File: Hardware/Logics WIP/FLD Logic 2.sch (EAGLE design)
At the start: 82 parts

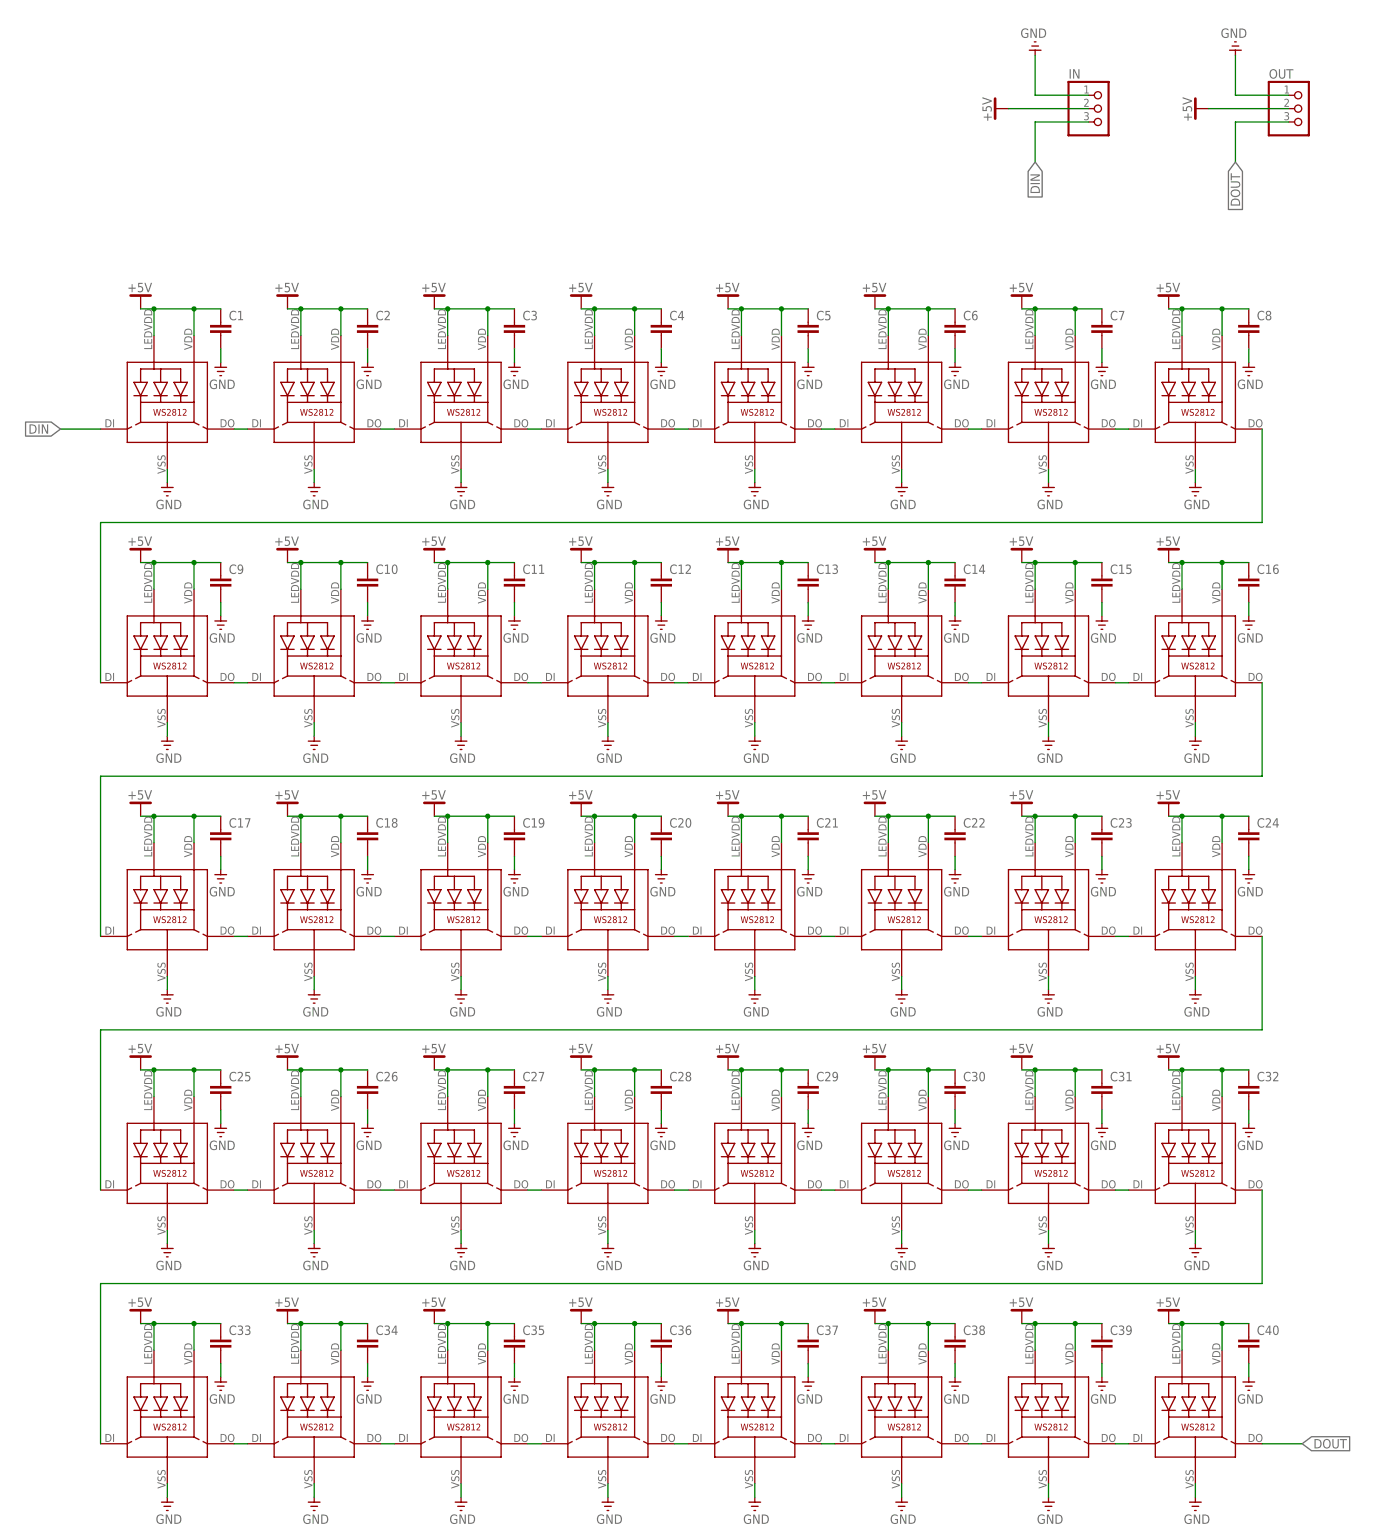
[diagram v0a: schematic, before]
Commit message: 
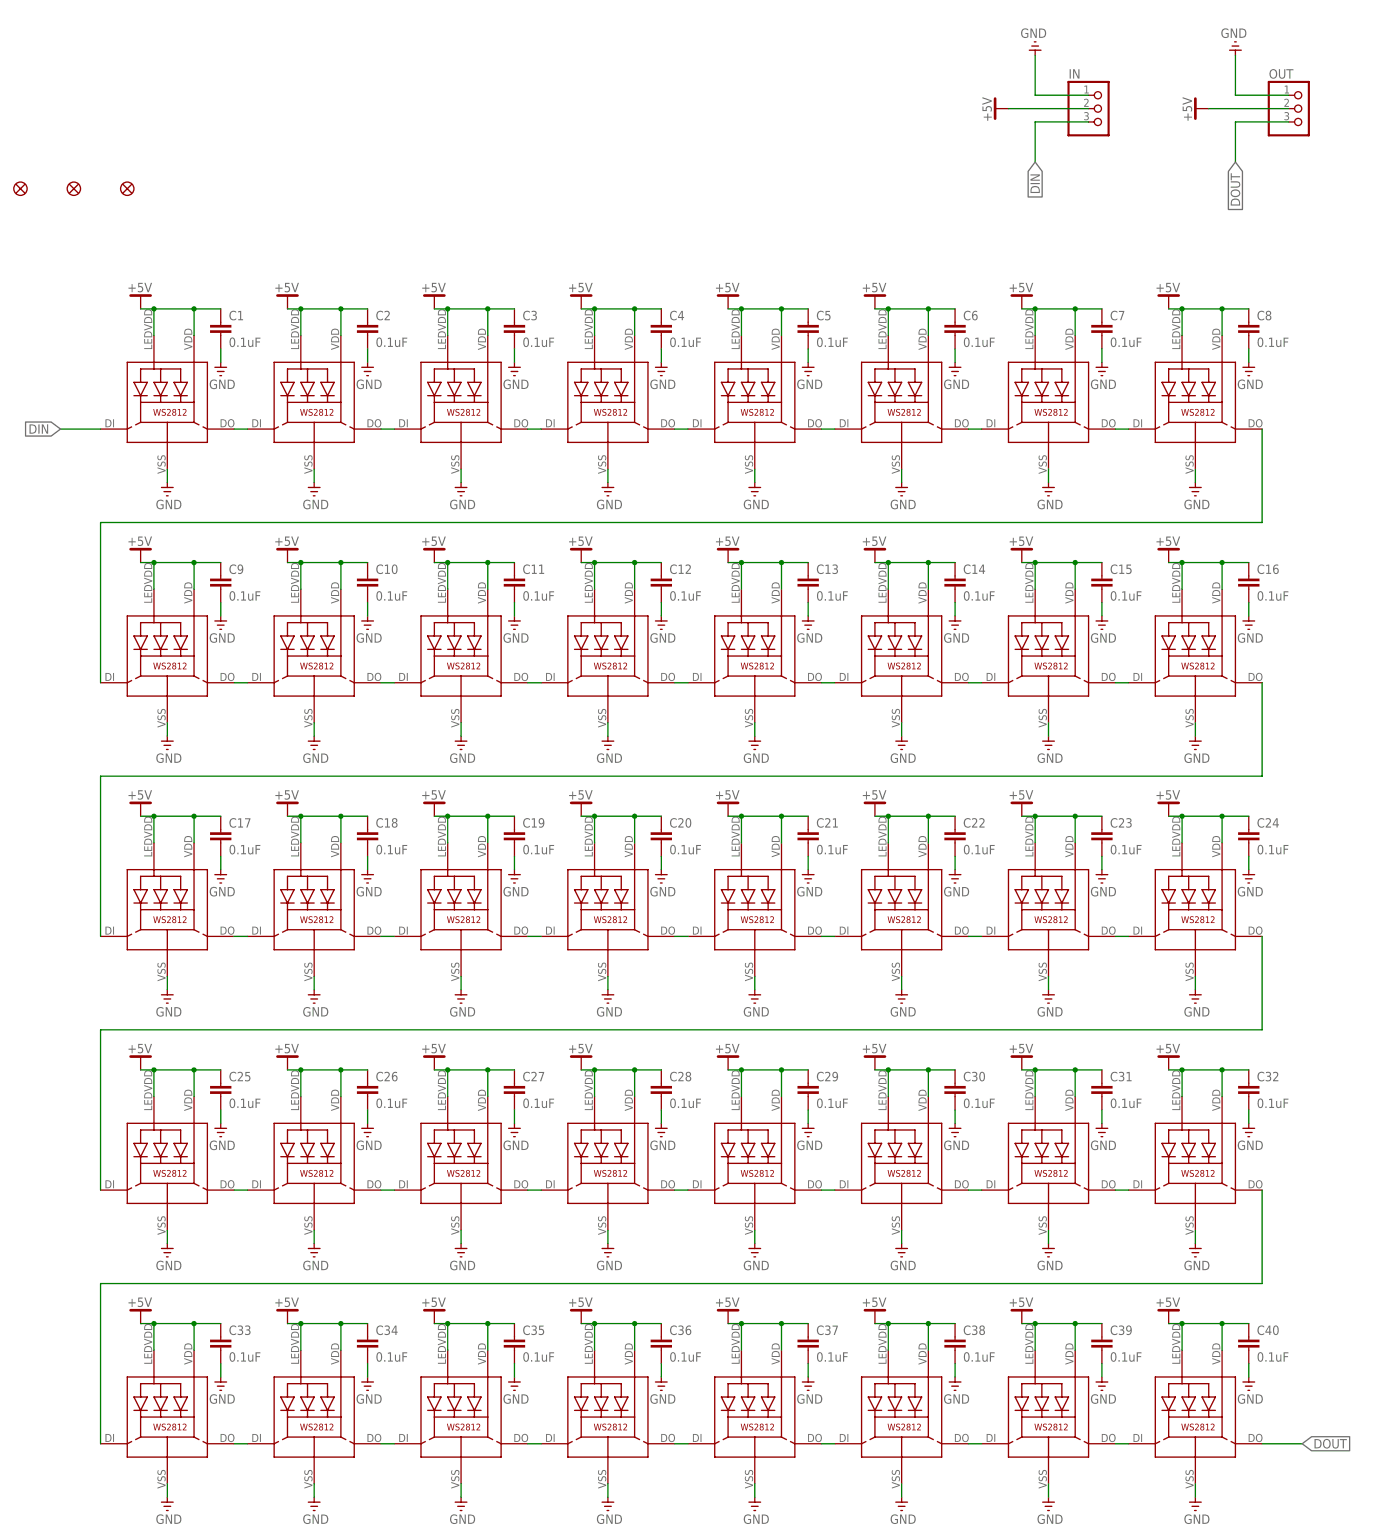
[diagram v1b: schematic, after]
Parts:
- added FID1, FID2, FID3: FIDUCIAL1.5X3, SparkFun-Aesthetics:FIDUCIAL1.5X3
- C1, C10, C11, C12, C13, C14, C15, C16, C17, C18, C19, C2, C20, C21, C22, C23, C24, C25, C26, C27, C28, C29, C3, C30, C31, C32, C33, C34, C35, C36, C37, C38, C39, C4, C40, C5, C6, C7, C8, C9: value (none) -> 0.1uF

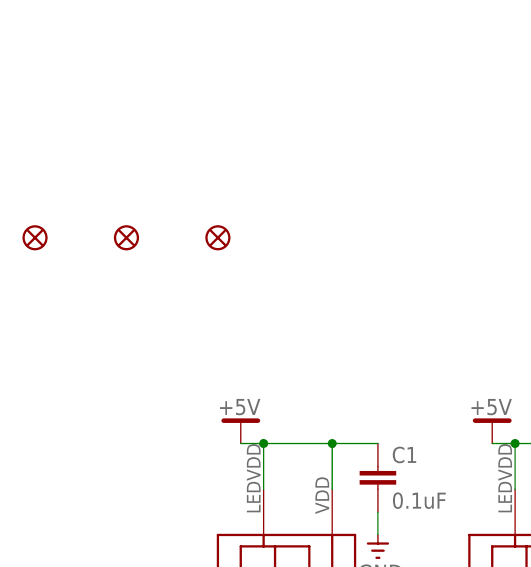
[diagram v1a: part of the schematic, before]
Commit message: 
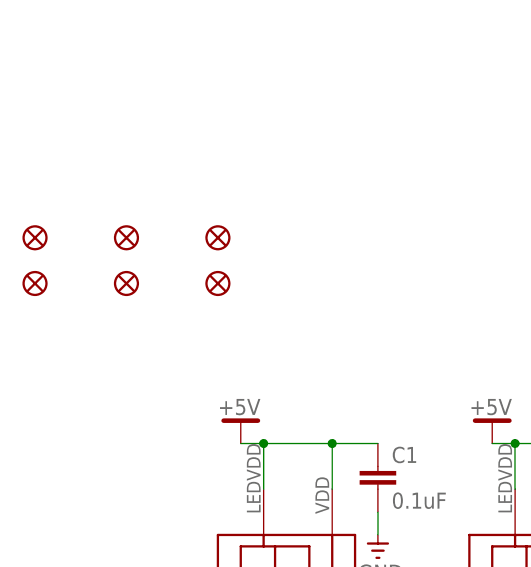
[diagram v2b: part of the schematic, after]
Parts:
- added FID4, FID5, FID6: FIDUCIAL1.5X3, SparkFun-Aesthetics:FIDUCIAL1.5X3
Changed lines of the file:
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@@
 <class number="0" name="default" width="0" drill="0">
 </class>
-<class number="1" name="supply" width="0.3048" drill="0.1524">
+<class number="1" name="supply" width="0.4064" drill="0.3302">
 <clearance class="1" value="0.2032"/>
 </class>
@@
 <part name="FID2" library="SparkFun-Aesthetics" deviceset="FIDUCIAL" device="1.5X3"/>
 <part name="FID3" library="SparkFun-Aesthetics" deviceset="FIDUCIAL" device="1.5X3"/>
+<part name="FID4" library="SparkFun-Aesthetics" deviceset="FIDUCIAL" device="1.5X3"/>
+<part name="FID5" library="SparkFun-Aesthetics" deviceset="FIDUCIAL" device="1.5X3"/>
+<part name="FID6" library="SparkFun-Aesthetics" deviceset="FIDUCIAL" device="1.5X3"/>
 </parts>
 <sheets>
@@
 <instance part="FID2" gate="G$1" x="91.44" y="198.12"/>
 <instance part="FID3" gate="G$1" x="101.6" y="198.12"/>
+<instance part="FID4" gate="G$1" x="81.28" y="193.04"/>
+<instance part="FID5" gate="G$1" x="91.44" y="193.04"/>
+<instance part="FID6" gate="G$1" x="101.6" y="193.04"/>
 </instances>
 <busses>

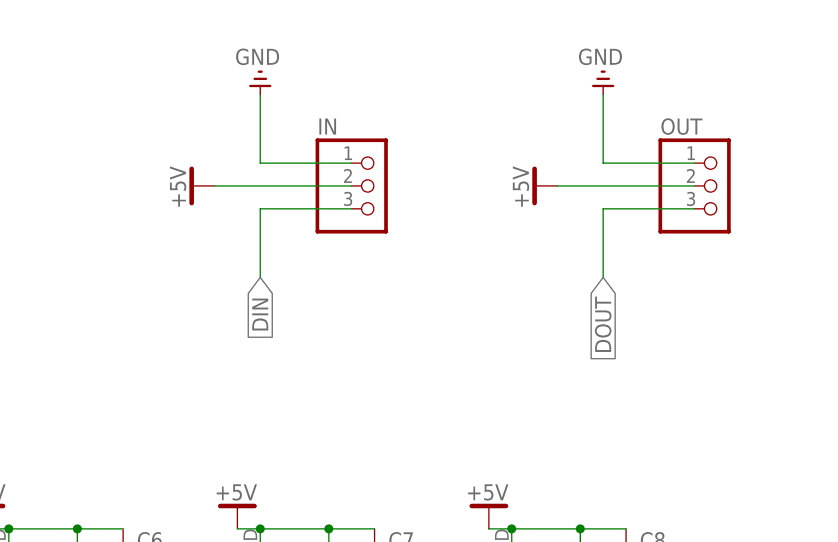
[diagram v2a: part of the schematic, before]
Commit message: 
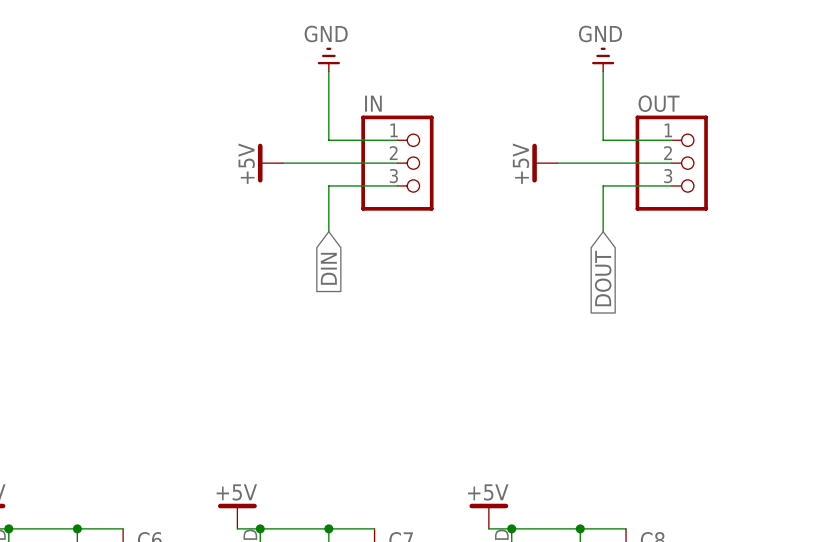
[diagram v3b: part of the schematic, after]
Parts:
- IN, OUT: device pinhead:PINHD-1X3 -> adafruit:PINHD-1X3
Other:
- moved on the sheet: IN, OUT
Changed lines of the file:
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@@
 </classes>
 <parts>
-<part name="IN" library="pinhead" deviceset="PINHD-1X3" device=""/>
-<part name="OUT" library="pinhead" deviceset="PINHD-1X3" device=""/>
-<part name="V9" library="supply0" deviceset="+5V" device=""/>
-<part name="GND3" library="supply0" deviceset="GND" device=""/>
-<part name="V42" library="supply0" deviceset="+5V" device=""/>
-<part name="GND82" library="supply0" deviceset="GND" device=""/>
 <part name="LED1" library="rseries" deviceset="WS2812" device=""/>
 <part name="C1" library="SparkFun-Capacitors" deviceset="CAP" device="0805" value="0.1uF"/>
@@
 <part name="FID5" library="SparkFun-Aesthetics" deviceset="FIDUCIAL" device="1.5X3"/>
 <part name="FID6" library="SparkFun-Aesthetics" deviceset="FIDUCIAL" device="1.5X3"/>
+<part name="IN" library="adafruit" deviceset="PINHD-1X3" device=""/>
+<part name="GND83" library="supply0" deviceset="GND" device=""/>
+<part name="V43" library="supply0" deviceset="+5V" device=""/>
+<part name="OUT" library="adafruit" deviceset="PINHD-1X3" device=""/>
+<part name="GND84" library="supply0" deviceset="GND" device=""/>
+<part name="V44" library="supply0" deviceset="+5V" device=""/>
 </parts>
 <sheets>
@@
 </plain>
 <instances>
-<instance part="IN" gate="A" x="287.02" y="213.36"/>
-<instance part="OUT" gate="A" x="325.12" y="213.36"/>
-<instance part="V9" gate="1" x="266.7" y="213.36" rot="R90"/>
-<instance part="GND3" gate="1" x="274.32" y="226.06" rot="R180"/>
-<instance part="V42" gate="1" x="304.8" y="213.36" rot="R90"/>
-<instance part="GND82" gate="1" x="312.42" y="226.06" rot="R180"/>
 <instance part="LED1" gate="G$1" x="109.22" y="154.94"/>
 <instance part="C1" gate="G$1" x="119.38" y="170.18"/>
@@
 <instance part="FID5" gate="G$1" x="91.44" y="193.04"/>
 <instance part="FID6" gate="G$1" x="101.6" y="193.04"/>
+<instance part="IN" gate="A" x="292.1" y="215.9"/>
+<instance part="GND83" gate="1" x="281.94" y="228.6" rot="R180"/>
+<instance part="V43" gate="1" x="274.32" y="215.9" rot="R90"/>
+<instance part="OUT" gate="A" x="322.58" y="215.9"/>
+<instance part="GND84" gate="1" x="312.42" y="228.6" rot="R180"/>
+<instance part="V44" gate="1" x="304.8" y="215.9" rot="R90"/>
 </instances>
 <busses>
@@
 <net name="GND" class="1">
 <segment>
-<pinref part="IN" gate="A" pin="1"/>
-<wire x1="284.48" y1="215.9" x2="274.32" y2="215.9" width="0.1524" layer="91"/>
-<wire x1="274.32" y1="215.9" x2="274.32" y2="223.52" width="0.1524" layer="91"/>
-<pinref part="GND3" gate="1" pin="GND"/>
-</segment>
-<segment>
-<pinref part="OUT" gate="A" pin="1"/>
-<wire x1="322.58" y1="215.9" x2="312.42" y2="215.9" width="0.1524" layer="91"/>
-<wire x1="312.42" y1="215.9" x2="312.42" y2="223.52" width="0.1524" layer="91"/>
-<pinref part="GND82" gate="1" pin="GND"/>
-</segment>
-<segment>
 <pinref part="C1" gate="G$1" pin="2"/>
 <wire x1="119.38" y1="167.64" x2="119.38" y2="165.1" width="0.1524" layer="91"/>
@@
 <wire x1="304.8" y1="-48.26" x2="304.8" y2="-50.8" width="0.1524" layer="91"/>
 </segment>
+<segment>
+<pinref part="IN" gate="A" pin="1"/>
+<pinref part="GND83" gate="1" pin="GND"/>
+<wire x1="289.56" y1="218.44" x2="281.94" y2="218.44" width="0.1524" layer="91"/>
+<wire x1="281.94" y1="218.44" x2="281.94" y2="226.06" width="0.1524" layer="91"/>
+</segment>
+<segment>
+<pinref part="OUT" gate="A" pin="1"/>
+<pinref part="GND84" gate="1" pin="GND"/>
+<wire x1="320.04" y1="218.44" x2="312.42" y2="218.44" width="0.1524" layer="91"/>
+<wire x1="312.42" y1="218.44" x2="312.42" y2="226.06" width="0.1524" layer="91"/>
+</segment>
 </net>
 <net name="+5V" class="1">
-<segment>
-<pinref part="IN" gate="A" pin="2"/>
-<wire x1="284.48" y1="213.36" x2="269.24" y2="213.36" width="0.1524" layer="91"/>
-<pinref part="V9" gate="1" pin="+5V"/>
-</segment>
-<segment>
-<pinref part="OUT" gate="A" pin="2"/>
-<wire x1="322.58" y1="213.36" x2="307.34" y2="213.36" width="0.1524" layer="91"/>
-<pinref part="V42" gate="1" pin="+5V"/>
-</segment>
 <segment>
 <pinref part="V1" gate="1" pin="+5V"/>
@@
 <junction x="309.88" y="-17.78"/>
 </segment>
+<segment>
+<pinref part="IN" gate="A" pin="2"/>
+<wire x1="289.56" y1="215.9" x2="276.86" y2="215.9" width="0.1524" layer="91"/>
+<pinref part="V43" gate="1" pin="+5V"/>
+</segment>
+<segment>
+<pinref part="OUT" gate="A" pin="2"/>
+<wire x1="320.04" y1="215.9" x2="307.34" y2="215.9" width="0.1524" layer="91"/>
+<pinref part="V44" gate="1" pin="+5V"/>
+</segment>
 </net>
 <net name="DOUT" class="0">
-<segment>
-<pinref part="OUT" gate="A" pin="3"/>
-<wire x1="322.58" y1="210.82" x2="312.42" y2="210.82" width="0.1524" layer="91"/>
-<wire x1="312.42" y1="210.82" x2="312.42" y2="203.2" width="0.1524" layer="91"/>
-<label x="312.42" y="203.2" size="1.778" layer="95" rot="R270" xref="yes"/>
-</segment>
 <segment>
 <pinref part="LED40" gate="G$1" pin="DO"/>
@@
 <label x="325.12" y="-40.64" size="1.778" layer="95" xref="yes"/>
 </segment>
+<segment>
+<pinref part="OUT" gate="A" pin="3"/>
+<wire x1="320.04" y1="213.36" x2="312.42" y2="213.36" width="0.1524" layer="91"/>
+<wire x1="312.42" y1="213.36" x2="312.42" y2="208.28" width="0.1524" layer="91"/>
+<label x="312.42" y="208.28" size="1.778" layer="95" rot="R270" xref="yes"/>
+</segment>
 </net>
 <net name="DIN" class="0">
-<segment>
-<pinref part="IN" gate="A" pin="3"/>
-<wire x1="284.48" y1="210.82" x2="274.32" y2="210.82" width="0.1524" layer="91"/>
-<wire x1="274.32" y1="210.82" x2="274.32" y2="203.2" width="0.1524" layer="91"/>
-<label x="274.32" y="203.2" size="1.778" layer="95" rot="R270" xref="yes"/>
-</segment>
 <segment>
 <pinref part="LED1" gate="G$1" pin="DI"/>
@@
 <label x="88.9" y="152.4" size="1.778" layer="95" rot="R180" xref="yes"/>
 </segment>
+<segment>
+<pinref part="IN" gate="A" pin="3"/>
+<wire x1="289.56" y1="213.36" x2="281.94" y2="213.36" width="0.1524" layer="91"/>
+<wire x1="281.94" y1="213.36" x2="281.94" y2="208.28" width="0.1524" layer="91"/>
+<label x="281.94" y="208.28" size="1.778" layer="95" rot="R270" xref="yes"/>
+</segment>
 </net>

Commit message: 
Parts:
- removed FID1, FID2, FID3, FID4, FID5, FID6: FIDUCIAL1.5X3, SparkFun-Aesthetics:FIDUCIAL1.5X3
- added FID10, FID11, FID12, FID7, FID8, FID9: (no value), SmallBatchLibPre1:FIDUCIAL
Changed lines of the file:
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@@
 <part name="GND80" library="supply0" deviceset="GND" device=""/>
 <part name="GND81" library="supply0" deviceset="GND" device=""/>
-<part name="FID1" library="SparkFun-Aesthetics" deviceset="FIDUCIAL" device="1.5X3"/>
-<part name="FID2" library="SparkFun-Aesthetics" deviceset="FIDUCIAL" device="1.5X3"/>
-<part name="FID3" library="SparkFun-Aesthetics" deviceset="FIDUCIAL" device="1.5X3"/>
-<part name="FID4" library="SparkFun-Aesthetics" deviceset="FIDUCIAL" device="1.5X3"/>
-<part name="FID5" library="SparkFun-Aesthetics" deviceset="FIDUCIAL" device="1.5X3"/>
-<part name="FID6" library="SparkFun-Aesthetics" deviceset="FIDUCIAL" device="1.5X3"/>
 <part name="IN" library="adafruit" deviceset="PINHD-1X3" device=""/>
 <part name="GND83" library="supply0" deviceset="GND" device=""/>
@@
 <part name="GND84" library="supply0" deviceset="GND" device=""/>
 <part name="V44" library="supply0" deviceset="+5V" device=""/>
+<part name="FID7" library="SmallBatchLibPre1" deviceset="FIDUCIAL" device=""/>
+<part name="FID8" library="SmallBatchLibPre1" deviceset="FIDUCIAL" device=""/>
+<part name="FID9" library="SmallBatchLibPre1" deviceset="FIDUCIAL" device=""/>
+<part name="FID10" library="SmallBatchLibPre1" deviceset="FIDUCIAL" device=""/>
+<part name="FID11" library="SmallBatchLibPre1" deviceset="FIDUCIAL" device=""/>
+<part name="FID12" library="SmallBatchLibPre1" deviceset="FIDUCIAL" device=""/>
 </parts>
 <sheets>
@@
 <instance part="GND80" gate="1" x="314.96" y="-30.48"/>
 <instance part="GND81" gate="1" x="304.8" y="-53.34"/>
-<instance part="FID1" gate="G$1" x="81.28" y="198.12"/>
-<instance part="FID2" gate="G$1" x="91.44" y="198.12"/>
-<instance part="FID3" gate="G$1" x="101.6" y="198.12"/>
-<instance part="FID4" gate="G$1" x="81.28" y="193.04"/>
-<instance part="FID5" gate="G$1" x="91.44" y="193.04"/>
-<instance part="FID6" gate="G$1" x="101.6" y="193.04"/>
 <instance part="IN" gate="A" x="292.1" y="215.9"/>
 <instance part="GND83" gate="1" x="281.94" y="228.6" rot="R180"/>
@@
 <instance part="GND84" gate="1" x="312.42" y="228.6" rot="R180"/>
 <instance part="V44" gate="1" x="304.8" y="215.9" rot="R90"/>
+<instance part="FID7" gate="G$1" x="119.38" y="200.66"/>
+<instance part="FID8" gate="G$1" x="132.08" y="200.66"/>
+<instance part="FID9" gate="G$1" x="144.78" y="200.66"/>
+<instance part="FID10" gate="G$1" x="119.38" y="193.04"/>
+<instance part="FID11" gate="G$1" x="132.08" y="193.04"/>
+<instance part="FID12" gate="G$1" x="144.78" y="193.04"/>
 </instances>
 <busses>
